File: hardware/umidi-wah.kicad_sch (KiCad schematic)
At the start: 31 parts, among them J1 Conn_01x02, J2 Conn_01x02, J3 Conn_02x05_Odd_Even, J4 Conn_01x02, J5 Input, J6 Output, J7 Conn_02x05_Odd_Even, J8 Conn_02x05_Odd_Even, K1 G6K-2P-Y-DC5, Q3 KSC1815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

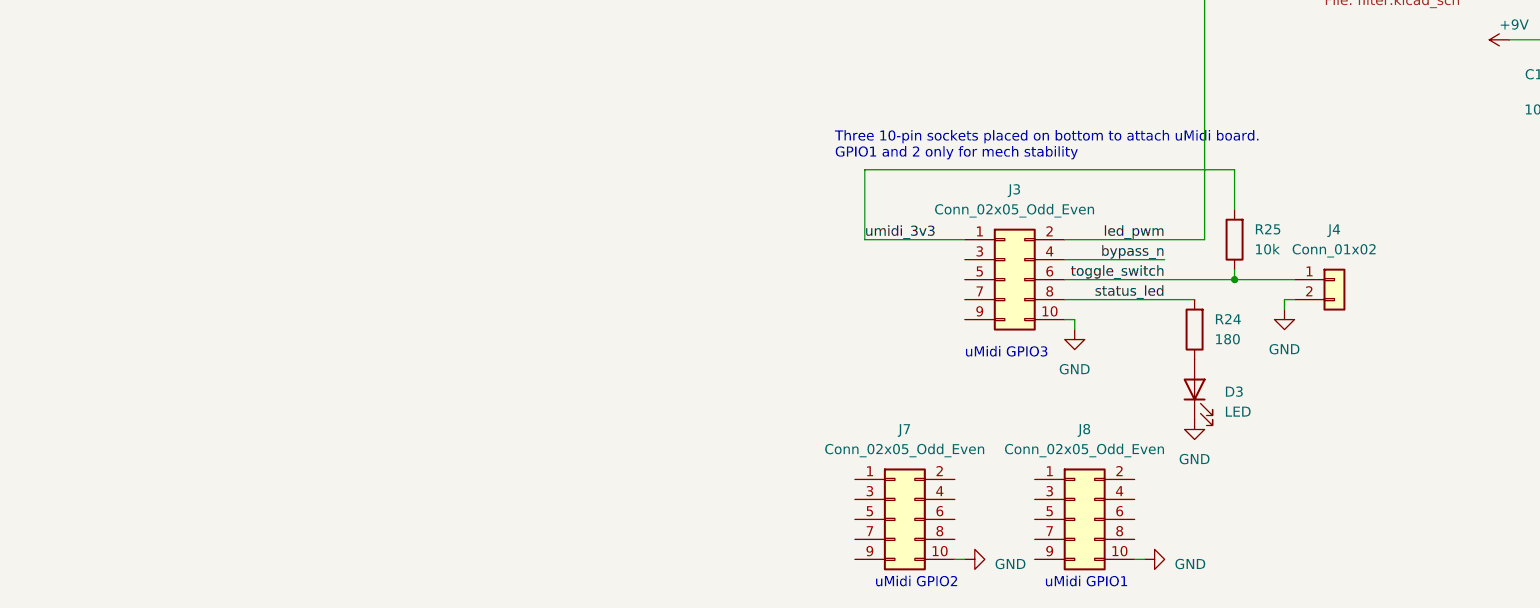
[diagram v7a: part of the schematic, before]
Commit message: Add top pin headers
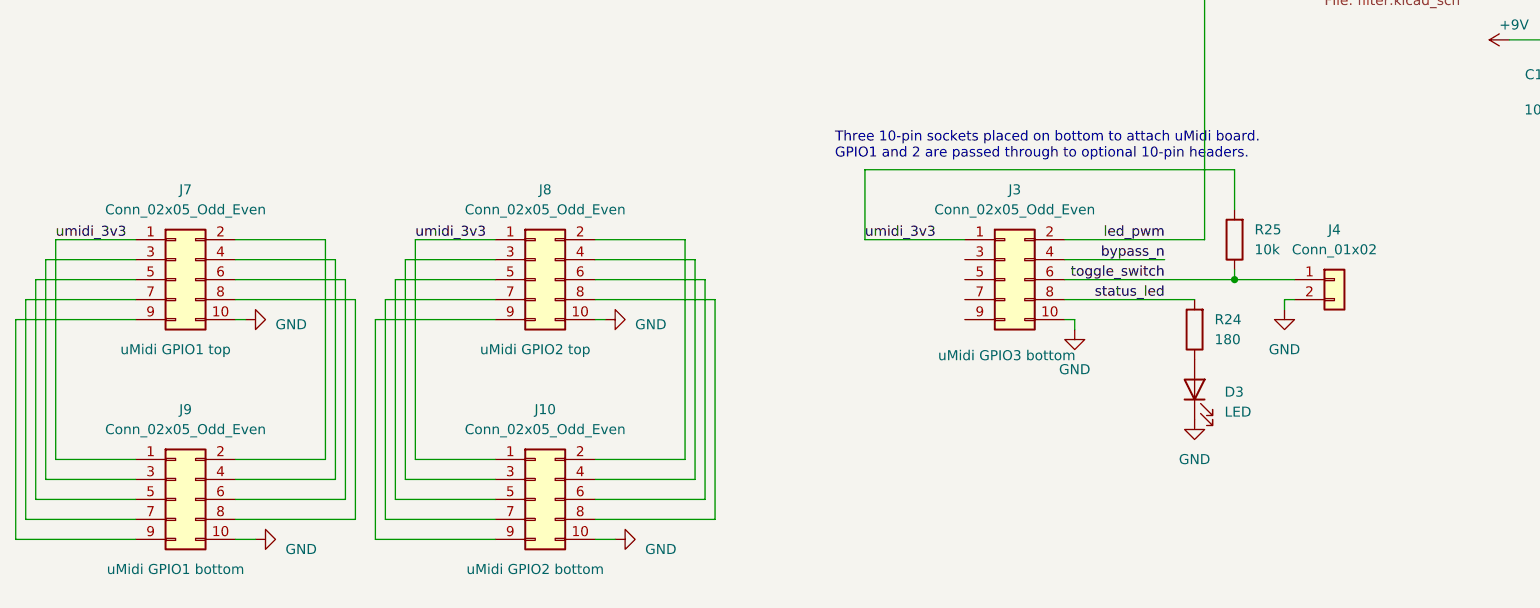
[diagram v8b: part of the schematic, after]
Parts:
- added J10, J9: Conn_02x05_Odd_Even, Connector_PinSocket_2.54mm:PinSocket_2x05_P2.54mm_Vertical, symbol Connector_Generic:Conn_02x05_Odd_Even
- J3: Function (none) -> uMidi GPIO3 bottom
- J7: Function (none) -> uMidi GPIO1 top
- J8: Function (none) -> uMidi GPIO2 top
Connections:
- net GND: now also J10.10 (Pin_10), J9.10 (Pin_10)
- net umidi_3v3: now also J7.1 (Pin_1), J8.1 (Pin_1), J10.1 (Pin_1), J9.1 (Pin_1)
- net at J8.2 (Pin_2): now also J10.2 (Pin_2)
- net at J8.3 (Pin_3): now also J10.3 (Pin_3)
- net at J8.4 (Pin_4): now also J10.4 (Pin_4)
- net at J8.5 (Pin_5): now also J10.5 (Pin_5)
- net at J8.6 (Pin_6): now also J10.6 (Pin_6)
- net at J8.7 (Pin_7): now also J10.7 (Pin_7)
- net at J8.8 (Pin_8): now also J10.8 (Pin_8)
- net at J8.9 (Pin_9): now also J10.9 (Pin_9)
- net at J7.2 (Pin_2): now also J9.2 (Pin_2)
- net at J7.3 (Pin_3): now also J9.3 (Pin_3)
- net at J7.4 (Pin_4): now also J9.4 (Pin_4)
- net at J7.5 (Pin_5): now also J9.5 (Pin_5)
- net at J7.6 (Pin_6): now also J9.6 (Pin_6)
- net at J7.7 (Pin_7): now also J9.7 (Pin_7)
- net at J7.8 (Pin_8): now also J9.8 (Pin_8)
- net at J7.9 (Pin_9): now also J9.9 (Pin_9)
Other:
- note added: "Three 10-pin sockets placed on bottom to attach uMidi board. GPIO1 and 2 are passed through to optional 10-pin headers."
- note removed: "Three 10-pin sockets placed on bottom to attach uMidi board. GPIO1 and 2 only for mech stability"
- note removed: "uMidi GPIO1"
- note removed: "uMidi GPIO2"
- note removed: "uMidi GPIO3"
- moved on the sheet: J8
